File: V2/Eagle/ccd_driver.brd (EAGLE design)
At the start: 60 x 60 mm, 48 parts, among them IC1 74HC04D, IC3 FT232RL, J1 USB-MINIB-5PIN, Q1 BC214, U2 MK02FN128VLF10

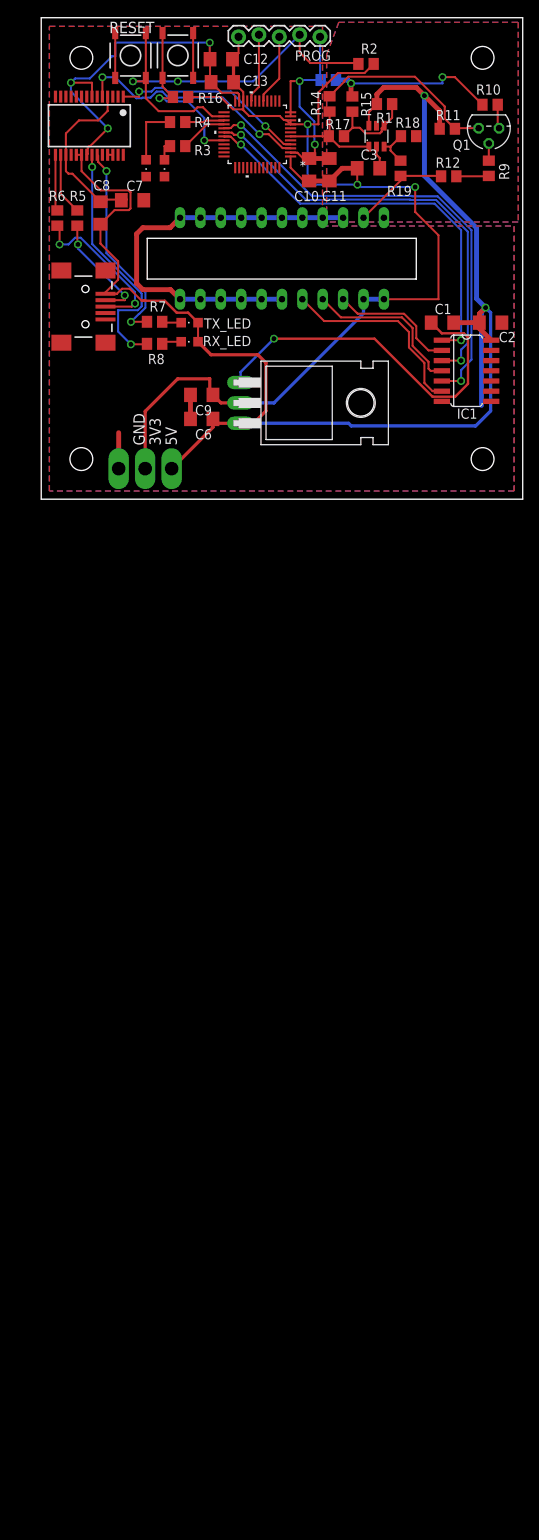
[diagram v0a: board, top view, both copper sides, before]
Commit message: Changed fM,SH,ICG pins to match with timers, added TODO list, cleaned up schematics and add them to different sheets
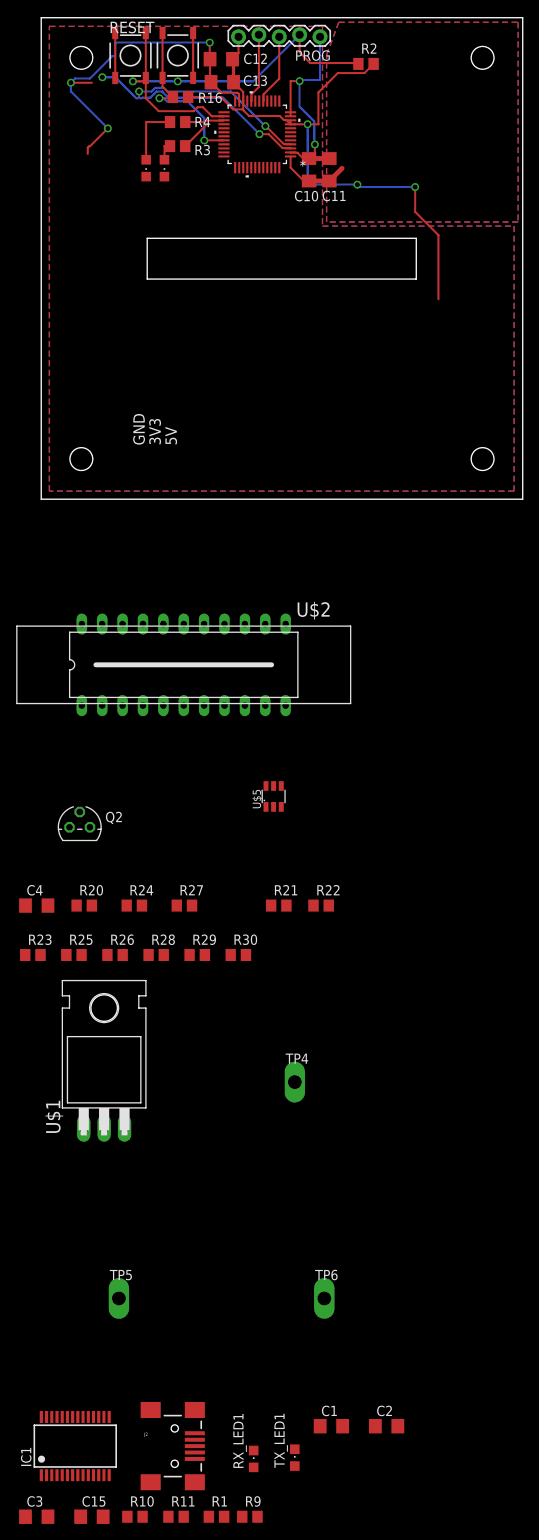
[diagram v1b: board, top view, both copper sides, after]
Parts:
- removed C6, C7, C8: 0.1 µF, resistor:C1206
- removed C9: 10uF, resistor:C1206
- removed IC3: FT232RL, ftdichip:SSOP28
- removed J1: USB-MINIB-5PIN, SparkFun-Connectors:USB-MINIB
- removed Q1: BC214, transistor-pnp:TO92
- removed R12, R13, R14: 0, resistor:R0805
- removed R15: 5.9k, resistor:R0805
- removed R17, R18: 11k, resistor:R0805
- removed R19: 10.5k, resistor:R0805
- removed R5, R6: 22, resistor:R0805
- removed R7, R8: 1k, resistor:R0805
- removed RX_LED, TX_LED: (no value), led:CHIPLED_0805
- removed TP1, TP2, TP3: TPPAD1-17Y, testpad:P1-17Y
- removed U$3: LTC6252, ccd:TSOT23-6
- removed U$4: LD1117V33, ccd:TO220H
- added C15: 10uF, resistor:C1206
- added C4: 0.1µF, resistor:C1206
- added J2: USB-MINIB-5PIN, SparkFun-Connectors:USB-MINIB
- added Q2: BC214, transistor-pnp:TO92
- added R20: 69.8k, resistor:R0805
- added R21: 5.9k, resistor:R0805
- added R22, R23: 11k, resistor:R0805
- added R24: 10.5k, resistor:R0805
- added R25, R26: 150, resistor:R0805
- added R27: 2200, resistor:R0805
- added R28, R29, R30: 0, resistor:R0805
- added RX_LED1, TX_LED1: (no value), led:CHIPLED_0805
- added TP4, TP5, TP6: TPPAD1-17Y, testpad:P1-17Y
- added U$2: TCD1304, ccd:TCD1304
- added U$5: LTC6252, ccd:TSOT23-6
- C2: value 10uF -> 0.1 µF
- C3: value 0.1µF -> 0.1 µF
- IC1: value 74HC04D -> FT232RL; device 74xx-eu:SO14 -> ftdichip:SSOP28
- R1: value 69.8k -> 22
- R10: value 150 -> 1k
- R11: value 2200 -> 1k
- R9: value 150 -> 22
- U$1: value TCD1304 -> LD1117V33; device ccd:TCD1304 -> ccd:TO220H
- moved R10 181.4 mm to (11.7, -126.8), turned to 0 degrees
- moved R1 177.3 mm to (21.8, -126.8), turned to 0 degrees
- moved R11 176.2 mm to (16.8, -126.8)
- moved C3 173.0 mm to (-0.56, -126.8)
- moved R9 170.7 mm to (26.0, -126.8), turned to 0 degrees
- moved IC1 142.6 mm to (4.24, -118.0), turned to 0 degrees
- moved C1 138.2 mm to (36.2, -115.5), turned to 0 degrees
- moved C2 138.1 mm to (43.0, -115.5)
- moved U$1 100.7 mm to (7.84, -68.2), flipped to the top
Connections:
- removed net BU: Q1.1, R11.2, R14.1
- removed net N$14: J1.D-, R5.2
- removed net N$16: J1.D+, R6.2
- removed net N$17: C7.1, C8.2, IC3.17, IC3.4
- removed net N$18: IC3.23, R7.1
- removed net N$19: IC3.16, R5.1
- removed net N$20: IC3.15, R6.1
- removed net N$21: IC3.22, R8.1
- removed net N$22: R8.2, RX_LED.C
- removed net N$23: R7.2, TX_LED.C
- new net BU1: Q2.1, R27.2, R30.1
- new net N$28: R23.2, R24.1, U$5.3
- new net N$29: R24.2, R28.1, U$2.21
- new net N$30: Q2.2, R25.1
- new net N$31: Q2.3, R26.1
- new net N$32: R25.2, R28.2
- new net N$6: R20.1, R21.2, R22.2, U$5.4
- net 3.3V: now also C15.1, C4.1, TP5.TP, U$2.1, U$2.2; no longer C3.1, C9.1, TP1.TP, U$1.1, U$4.2
- net 5V: now also C3.1, IC1.19, IC1.20, J2.VBUS, R20.2, R27.1, RX_LED1.A, TP4.TP, TX_LED1.A, U$1.3, U$5.6; no longer C1.1, C6.1, C8.1, IC1.14, IC3.19, IC3.20, J1.VBUS, R1.2, R11.1, RX_LED.A, TP2.TP, TX_LED.A, U$3.6, U$4.3
- net AGND: now also C4.2, R21.1, R23.1, R26.2, R29.1, U$2.10, U$2.11, U$2.12, U$2.13, U$2.14, U$2.15, U$2.16, U$2.17, U$2.18, U$2.19, U$2.20, U$2.22, U$2.6, U$2.7, U$2.8, U$2.9, U$5.2; no longer C3.2, R10.2, R13.1, R15.1, R18.1, U$1.10, U$1.11, U$1.12, U$1.13, U$1.14, U$1.15, U$1.16, U$1.17, U$1.18, U$1.19, U$1.20, U$1.22, U$1.6, U$1.7, U$1.8, U$1.9, U$3.2
- net FM: now also U$2.4, U2.34; no longer IC1.3, U2.30
- net GND: now also C15.2, C3.2, IC1.18, IC1.21, IC1.25, IC1.26, J2.GND, R29.2, TP6.TP, U$1.1; no longer C2.2, C6.2, C7.2, C9.2, IC3.18, IC3.21, IC3.25, IC3.26, IC3.7, J1.GND, R13.2, TP3.TP, U$4.1
- net ICG: now also U$2.3, U2.28; no longer IC1.1, U2.31
- net N$1: now also IC1.16, R1.1; no longer R18.2, R19.1, U$3.3
- net N$10: now also R11.2, RX_LED1.C; no longer R12.1, R19.2, U$1.21
- net N$11: now also U2.30; no longer U2.28
- net N$15: now also U2.29; no longer U2.27
- net N$2: now also IC1.15, R9.1; no longer IC1.2, U$1.3
- net N$24: now also R10.2, TX_LED1.C; no longer R12.2, R9.2
- net N$3: now also J2.D-, R1.2; no longer IC1.4, U$1.4
- net N$4: now also J2.D+, R9.2; no longer IC1.6, U$1.5
- net N$5: now also C1.1, C2.2, IC1.17, IC1.4; no longer Q1.2, R9.1
- net N$8: now also IC1.23, R10.1; no longer R1.1, R15.2, R17.2, U$3.4
- net N$9: now also IC1.22, R11.1; no longer Q1.3, R10.1
- net OS: now also R22.1, R30.2, U$5.1; no longer R14.2, R17.1, U$3.1, U2.6
- net PCRX: now also IC1.1; no longer IC3.1
- net PCTX: now also IC1.5; no longer IC3.5
- net SH: now also U$2.5, U2.27; no longer IC1.5, U2.29
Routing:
- net 5V: track 185.8 -> 0.00 mm, vias 2 -> 0
- net AGND: track 76.9 -> 0.00 mm, vias 2 -> 0
- net SH: track 58.2 -> 0.00 mm, vias 2 -> 0
- net 3.3V: track 143.9 -> 86.0 mm
- net GND: track 142.9 -> 86.3 mm, vias 6 -> 5
- net FM: track 54.4 -> 0.00 mm, vias 2 -> 0
- net ICG: track 50.5 -> 0.00 mm, vias 2 -> 0
- net N$21: track 31.5 -> 0.00 mm, vias 2 -> 0
- net N$18: track 26.1 -> 0.00 mm, vias 2 -> 0
- net N$4: track 24.7 -> 0.00 mm
- net BU: track 23.3 -> 0.00 mm
- net N$17: track 22.9 -> 0.00 mm
- net N$16: track 20.4 -> 0.00 mm, vias 2 -> 0
- net N$3: track 20.4 -> 0.00 mm
- net N$2: track 15.8 -> 0.00 mm
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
